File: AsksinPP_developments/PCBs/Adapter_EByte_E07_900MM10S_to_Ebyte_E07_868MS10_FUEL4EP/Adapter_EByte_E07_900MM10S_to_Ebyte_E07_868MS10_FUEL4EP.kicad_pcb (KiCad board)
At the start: 2 copper layers, 19 x 13 mm, 15 parts

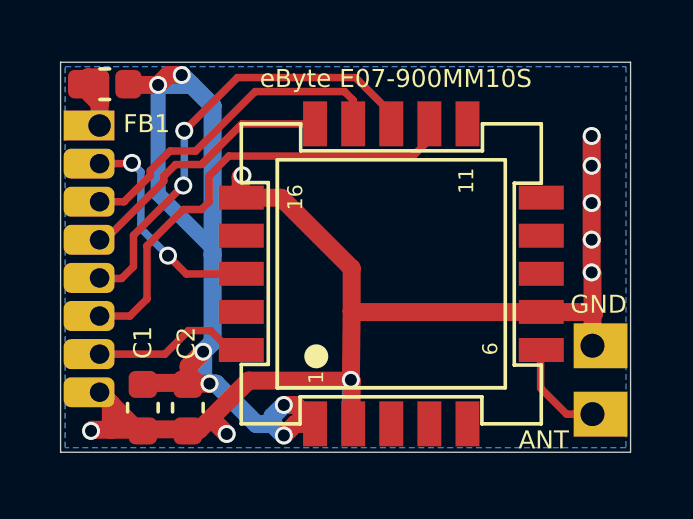
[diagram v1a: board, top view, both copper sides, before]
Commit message: PCBs/Adapter_EByte_E07_900MM10S_to_Ebyte_E07_868MS10_FUEL4EP: migration to KiCAD8; order of prototypes at JLCPCB
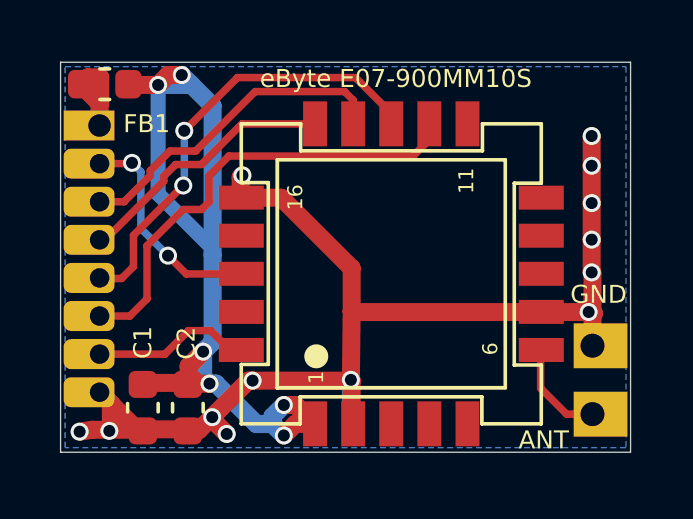
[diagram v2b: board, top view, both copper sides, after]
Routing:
- net GND: track 40.6 -> 41.0 mm, vias 9 -> 13
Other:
- board text added: "adapter E07 900MM10S V1.1 (C) FUEL4EP 09/2024"
- board text removed: "adapter E07 900MM10S V1.0 (C) FUEL4EP 06/2024"
